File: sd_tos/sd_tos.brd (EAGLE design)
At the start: 24.5 x 64.5 mm, 18 parts, among them IC1 MEGA16-A, IC3 74HCT595D

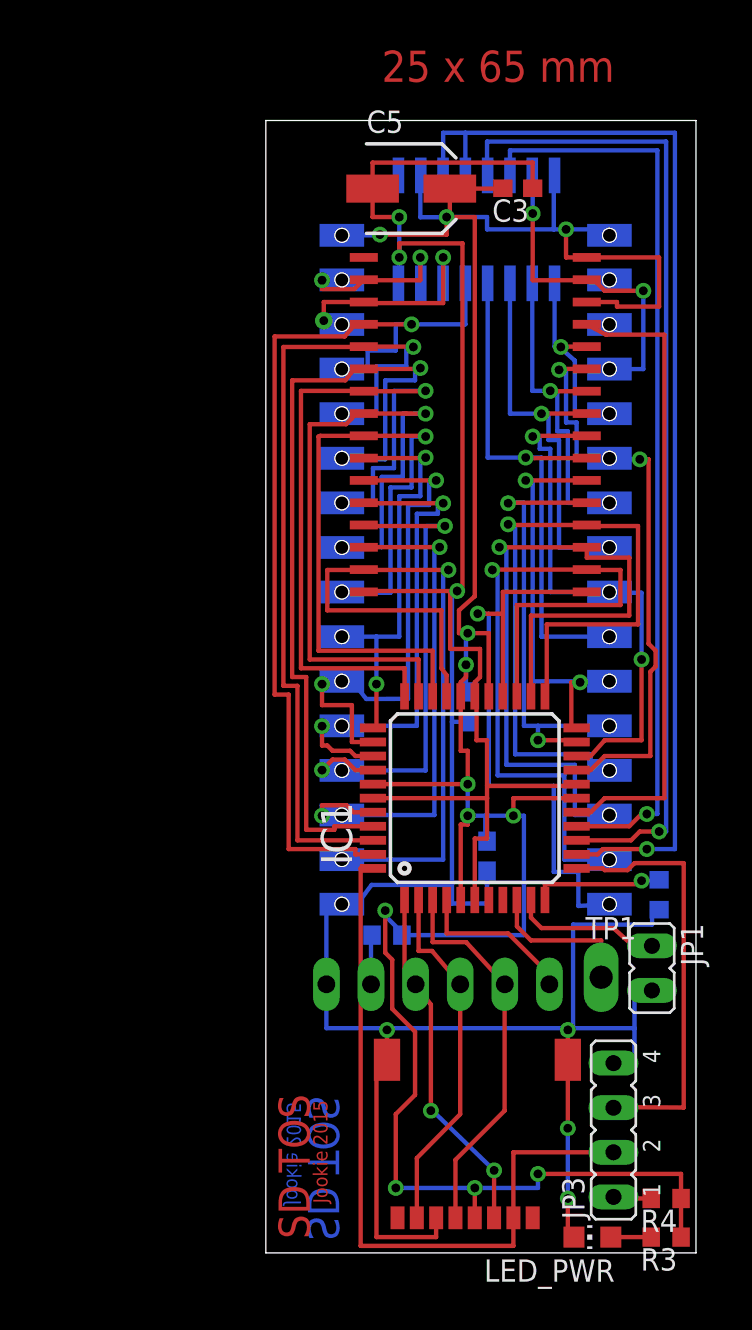
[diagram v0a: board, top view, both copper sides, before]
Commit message: added ST reset wire to master/slave connector, so you need to connect only single ST reset wire to the boards and they will share it
git-svn-id: https://subversion.assembla.com/svn/atarijookie/trunk@935 0d2ca917-fb58-4453-bb26-a698c01b0940
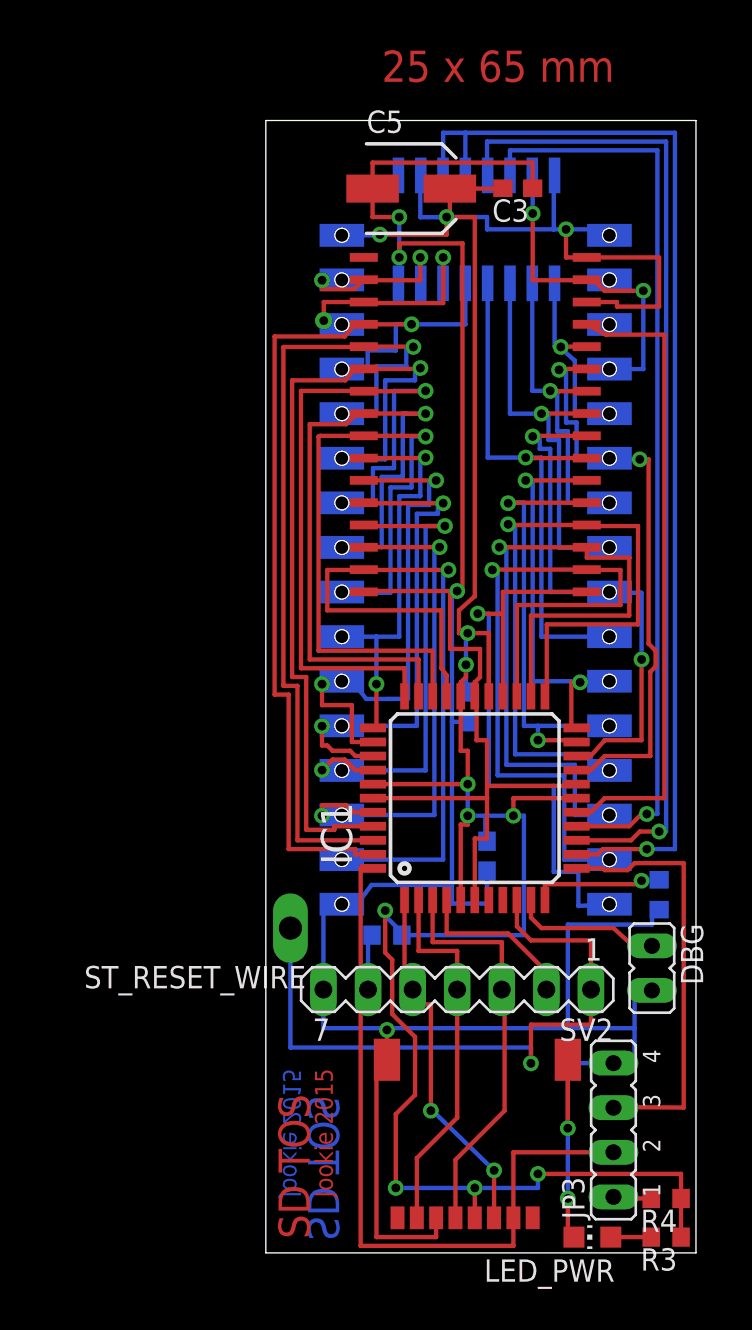
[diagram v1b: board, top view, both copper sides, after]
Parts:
- removed SV1: (no value), con-lstb:MA06-1
- removed TP1: PTR1PAD1-13Y, testpad:P1-13Y
- added ST_RESET_WIRE: PTR1PAD1-13Y, testpad:P1-13Y
- added SV2: (no value), con-lstb:MA07-1
- renumbered JP1 to DBG
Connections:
- net AVR_RESET: now also SV2.2; no longer SV1.1
- net GND: now also SV2.7; no longer SV1.6
- net MISO: now also SV2.4; no longer SV1.3
- net MOSI: now also SV2.5; no longer SV1.4
- net SCK: now also SV2.3; no longer SV1.2
- net SD_CS: now also SV2.6; no longer SV1.5
- net ST_RESET: now also ST_RESET_WIRE.TP, SV2.1; no longer TP1.TP
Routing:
- net ST_RESET: track 8.73 -> 37.9 mm, vias 0 -> 1
- net GND: track 184.1 -> 189.3 mm, vias 7 -> 6
- net SCK: track 22.0 -> 24.0 mm
- net MISO: track 20.5 -> 21.3 mm
- net MOSI: track 20.6 -> 21.3 mm

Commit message: activity SMD LED added on PCB - if you don't want to drag the external LED out
git-svn-id: https://subversion.assembla.com/svn/atarijookie/trunk@936 0d2ca917-fb58-4453-bb26-a698c01b0940
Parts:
- added LED_ACT: (no value), led:CHIP-LED0805
- added R5: 470 R, rcl:R0603
- moved R4 1.30 mm to (55.3, 7.40)
- moved JP3 1.22 mm to (52.5, 11.2)
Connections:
- new net N$2: LED_ACT.A, R5.1
- net SD_CS: now also LED_ACT.C
- net VCC: now also R5.2
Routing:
- net SD_CS: track 45.7 -> 51.6 mm
- net VCC: track 162.1 -> 164.5 mm
- net N$2: track 0.00 -> 2.30 mm
- net GND: track 189.3 -> 187.3 mm
- net BTN: track 24.2 -> 22.8 mm
- net A16: track 10.3 -> 11.4 mm
